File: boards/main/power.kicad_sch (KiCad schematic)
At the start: 19 parts, among them Q1 DMP2045U, U3 RT9080-33GJ5, U4 MCP73831T-2ACI_OT, U5 MAX17048G_T10

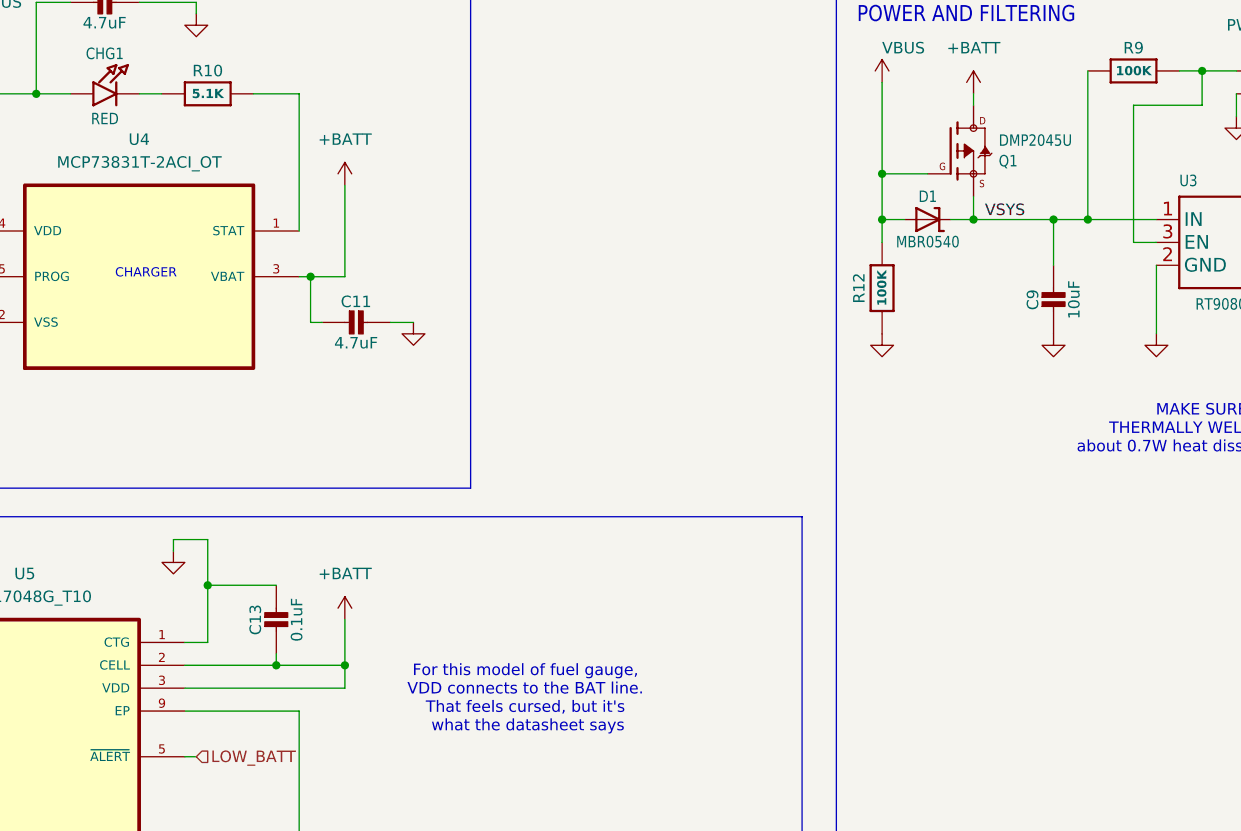
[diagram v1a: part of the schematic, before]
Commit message: Move the LED ring and haptic engine behind the charge controller, to prevent hot plug ringing from damaging things
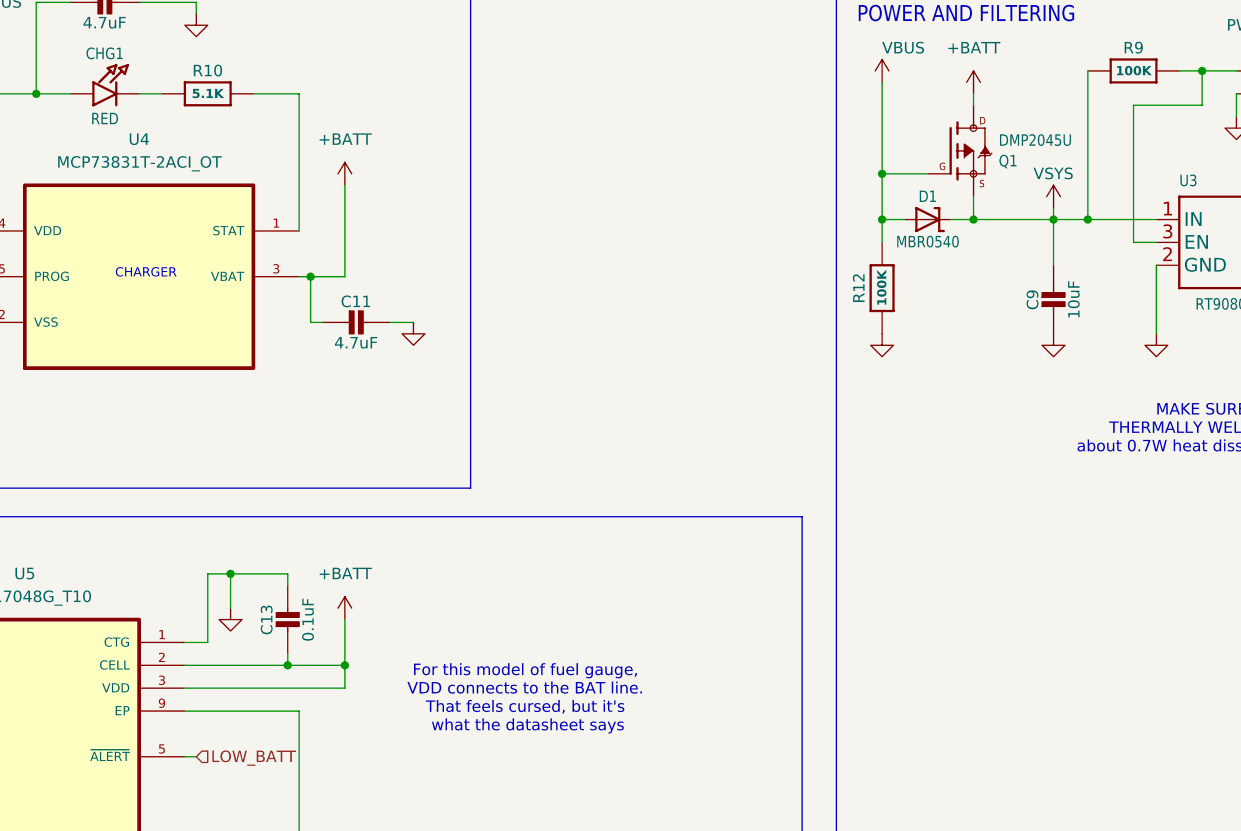
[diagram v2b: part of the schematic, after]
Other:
- moved on the sheet: C13
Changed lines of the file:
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@@
 	)
 	(junction
-		(at 78.74 96.52)
+		(at 93.98 105.41)
 		(diameter 0)
 		(color 0 0 0 0)
 	)
 	(junction
-		(at 93.98 105.41)
+		(at 153.67 55.88)
 		(diameter 0)
 		(color 0 0 0 0)
 	)
 	(junction
-		(at 153.67 55.88)
+		(at 87.63 105.41)
 		(diameter 0)
 		(color 0 0 0 0)
@@
 	)
 	(junction
-		(at 214.63 55.88)
+		(at 81.28 95.25)
 		(diameter 0)
 		(color 0 0 0 0)
 	)
 	(junction
-		(at 53.34 41.91)
+		(at 214.63 55.88)
 		(diameter 0)
 		(color 0 0 0 0)
 	)
 	(junction
-		(at 88.9 128.27)
+		(at 53.34 41.91)
 		(diameter 0)
 		(color 0 0 0 0)
 	)
 	(junction
-		(at 189.23 39.37)
+		(at 88.9 128.27)
 		(diameter 0)
 		(color 0 0 0 0)
 	)
 	(junction
-		(at 86.36 105.41)
+		(at 189.23 39.37)
 		(diameter 0)
 		(color 0 0 0 0)
@@
 	(wire
 		(pts
+			(xy 81.28 95.25) (xy 87.63 95.25)
+		)
+		(stroke
+			(width 0)
+			(type default)
+		)
+	)
+	(wire
+		(pts
 			(xy 93.98 107.95) (xy 93.98 105.41)
 		)
@@
 	(wire
 		(pts
-			(xy 78.74 96.52) (xy 78.74 102.87)
+			(xy 78.74 95.25) (xy 78.74 102.87)
+		)
+		(stroke
+			(width 0)
+			(type default)
+		)
+	)
+	(wire
+		(pts
+			(xy 87.63 95.25) (xy 87.63 96.52)
 		)
 		(stroke
@@
 	(wire
 		(pts
-			(xy 78.74 91.44) (xy 78.74 96.52)
-		)
-		(stroke
-			(width 0)
-			(type default)
-		)
-	)
-	(wire
-		(pts
 			(xy 49.53 62.23) (xy 53.34 62.23)
 		)
@@
 	(wire
 		(pts
-			(xy 78.74 96.52) (xy 86.36 96.52)
-		)
-		(stroke
-			(width 0)
-			(type default)
-		)
-	)
-	(wire
-		(pts
 			(xy 90.17 62.23) (xy 90.17 67.31)
 		)
@@
 	(wire
 		(pts
+			(xy 87.63 105.41) (xy 93.98 105.41)
+		)
+		(stroke
+			(width 0)
+			(type default)
+		)
+	)
+	(wire
+		(pts
 			(xy 214.63 68.58) (xy 214.63 71.12)
 		)
@@
 	(wire
 		(pts
-			(xy 76.2 105.41) (xy 86.36 105.41)
+			(xy 76.2 105.41) (xy 87.63 105.41)
 		)
 		(stroke
@@
 	(wire
 		(pts
-			(xy 74.93 91.44) (xy 78.74 91.44)
+			(xy 78.74 95.25) (xy 81.28 95.25)
 		)
 		(stroke
@@
 	(wire
 		(pts
+			(xy 172.72 54.61) (xy 172.72 55.88)
+		)
+		(stroke
+			(width 0)
+			(type default)
+		)
+	)
+	(wire
+		(pts
 			(xy 59.69 41.91) (xy 53.34 41.91)
 		)
@@
 	(wire
 		(pts
-			(xy 74.93 91.44) (xy 74.93 92.71)
+			(xy 81.28 95.25) (xy 81.28 99.06)
 		)
 		(stroke
@@
 	(wire
 		(pts
-			(xy 86.36 105.41) (xy 93.98 105.41)
-		)
-		(stroke
-			(width 0)
-			(type default)
-		)
-	)
-	(wire
-		(pts
 			(xy 181.61 43.18) (xy 181.61 58.42)
 		)
@@
 	(wire
 		(pts
-			(xy 86.36 104.14) (xy 86.36 105.41)
+			(xy 87.63 104.14) (xy 87.63 105.41)
 		)
 		(stroke
@@
 		)
 	)
-	(label "VSYS"
-		(at 165.1 55.88 0)
-		(effects
-			(font
-				(size 1.27 1.27)
-			)
-			(justify left bottom)
-		)
-	)
 	(hierarchical_label "SCL"
 		(shape input)
@@
 	(symbol
 		(lib_id "smart_compass_main:CAP_CERAMIC0603_NO")
-		(at 86.36 101.6 0)
+		(at 87.63 101.6 0)
 		(unit 1)
 		(body_style 1)
@@
 		(dnp no)
 		(property "Reference" "C13"
-			(at 84.07 100.35 90)
+			(at 85.34 100.35 90)
 			(show_name no)
 			(do_not_autoplace no)
@@
 		)
 		(property "Value" "0.1uF"
-			(at 88.66 100.35 90)
+			(at 89.93 100.35 90)
 			(show_name no)
 			(do_not_autoplace no)
@@
 		)
 		(property "Footprint" "Capacitor_SMD:C_0402_1005Metric"
-			(at 86.36 101.6 0)
+			(at 87.63 101.6 0)
 			(hide yes)
 			(show_name no)
@@
 		)
 		(property "Datasheet" "https://media.digikey.com/pdf/Data%20Sheets/Samsung%20PDFs/CL05B104KO5VPNC_Spec.pdf"
-			(at 86.36 101.6 0)
+			(at 87.63 101.6 0)
 			(hide yes)
 			(show_name no)
@@
 		)
 		(property "Description" ""
-			(at 86.36 101.6 0)
+			(at 87.63 101.6 0)
 			(hide yes)
 			(show_name no)
@@
 		)
 		(property "MPN" "CL05B104KO5VPNC"
-			(at 86.36 101.6 90)
+			(at 87.63 101.6 90)
 			(hide yes)
 			(show_name no)
@@
 		)
 		(property "PRICE" "0.02134"
-			(at 86.36 101.6 90)
+			(at 87.63 101.6 90)
 			(hide yes)
 			(show_name no)
@@
 		)
 		(property "MAXIMUM_PACKAGE_HIEGHT" ""
-			(at 86.36 101.6 90)
+			(at 87.63 101.6 90)
 			(hide yes)
 			(show_name no)
@@
 		)
 		(property "Manufacturer" "Samsung Electro-Mechanics"
-			(at 86.36 101.6 0)
+			(at 87.63 101.6 0)
 			(hide yes)
 			(show_name no)
@@
 		)
 		(property "DigiKey_PN" "1276-6844-1-ND"
-			(at 86.36 101.6 0)
+			(at 87.63 101.6 0)
 			(hide yes)
 			(show_name no)
@@
 		)
 		(property "Voltage" "16V"
-			(at 86.36 101.6 0)
+			(at 87.63 101.6 0)
 			(hide yes)
 			(show_name no)
@@
 		)
 		(property "Dielectric" "X7R"
-			(at 86.36 101.6 0)
+			(at 87.63 101.6 0)
 			(hide yes)
 			(show_name no)
@@
 		)
 		(property "DigiKey_Part_Number" ""
-			(at 86.36 101.6 90)
+			(at 87.63 101.6 90)
 			(hide yes)
 			(show_name no)
@@
 	(symbol
 		(lib_id "power:GND")
-		(at 74.93 92.71 0)
+		(at 81.28 99.06 0)
 		(unit 1)
 		(body_style 1)
@@
 		(fields_autoplaced yes)
 		(property "Reference" "#PWR038"
-			(at 74.93 99.06 0)
+			(at 81.28 105.41 0)
 			(hide yes)
 			(show_name no)
@@
 		)
 		(property "Value" "GND"
-			(at 74.93 97.79 0)
+			(at 81.28 104.14 0)
 			(hide yes)
 			(show_name no)
@@
 		)
 		(property "Footprint" ""
-			(at 74.93 92.71 0)
+			(at 81.28 99.06 0)
 			(hide yes)
 			(show_name no)
@@
 		)
 		(property "Datasheet" ""
-			(at 74.93 92.71 0)
+			(at 81.28 99.06 0)
 			(hide yes)
 			(show_name no)
@@
 		)
 		(property "Description" "Power symbol creates a global label with name \"GND\" , ground"
-			(at 74.93 92.71 0)
+			(at 81.28 99.06 0)
 			(hide yes)
 			(show_name no)
@@
 					(unit 1)
 				)
+			)
+		)
+	)
+	(symbol
+		(lib_id "power:+BATT")
+		(at 172.72 54.61 0)
+		(unit 1)
+		(body_style 1)
+		(exclude_from_sim no)
+		(in_bom yes)
+		(on_board yes)
+		(in_pos_files yes)
+		(dnp no)
+		(property "Reference" "#PWR079"
+			(at 172.72 58.42 0)
+			(hide yes)
+			(show_name no)
+			(do_not_autoplace no)
+			(effects
+				(font
+					(size 1.27 1.27)
+				)
+			)
+		)
+		(property "Value" "VSYS"
+			(at 172.72 50.8 0)
+			(show_name no)
+			(do_not_autoplace no)
+			(effects
+				(font
+					(size 1.27 1.27)
+				)
+			)
+		)
+		(property "Footprint" ""
+			(at 172.72 54.61 0)
+			(hide yes)
+			(show_name no)
+			(do_not_autoplace no)
+			(effects
+				(font
+					(size 1.27 1.27)
+				)
+			)
+		)
+		(property "Datasheet" ""
+			(at 172.72 54.61 0)
+			(hide yes)
+			(show_name no)
+			(do_not_autoplace no)
+			(effects
+				(font
+					(size 1.27 1.27)
+				)
+			)
+		)
+		(property "Description" "Power symbol creates a global label with name \"+BATT\""
+			(at 172.72 54.61 0)
+			(hide yes)
+			(show_name no)
+			(do_not_autoplace no)
+			(effects
+				(font
+					(size 1.27 1.27)
+				)
+			)
+		)
+		(pin "1"
+		)
+		(instances
+			(project "SmartCompass"
+				(path "/0c161f28-8075-4403-a867-35208f463636/44fc6246-5945-463a-870f-e1f278c176e3"
+					(reference "#PWR079")
+					(unit 1)
+				)

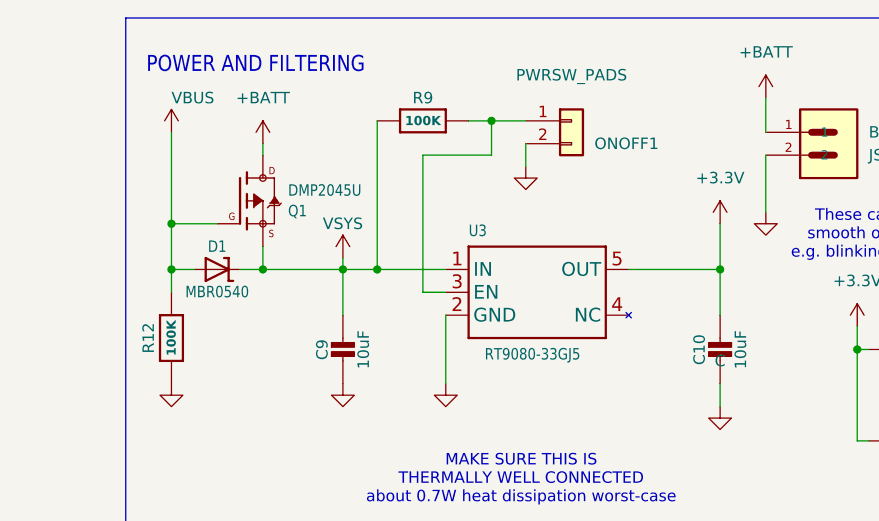
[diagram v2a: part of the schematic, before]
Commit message: Update components based on spice sim. Added another load-sharing schottky diode
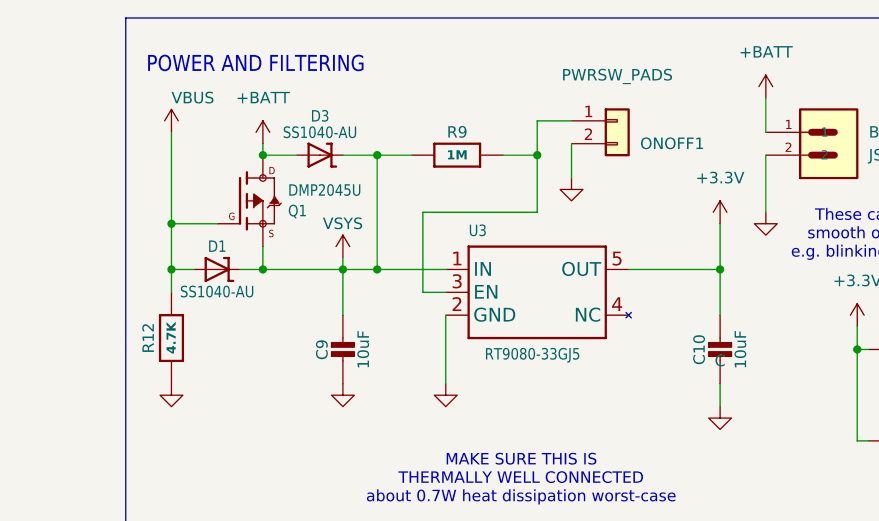
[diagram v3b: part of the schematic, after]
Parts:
- added D3: SS1040-AU, Diode_SMD:D_SOD-123, symbol smart_compass_main:DIODE-SCHOTTKYSOD-123
- D1: value MBR0540 -> SS1040-AU; DigiKey_PN MBR0540TPMSCT-ND -> 3757-SS1040-AU_R1_000A1CT-ND; MPN MBR0540-TP -> SS1040-AU_R1_000A1; Manufacturer MCC (Micro Commercial Components) -> Panjit International Inc.; PRICE 0.23 -> 0.18
- Q1: Sourcing_Note P-channel power mux between the battery and the LDO input: drain on +BATT, source on the LDO rail, gate on VBUS with a 100k pulldown, paired with the MBR0540 Schottky that feeds the rail from USB. Replaces the DMG3415U-7, which the manufacturer marks NOT RECOMMENDED FOR NEW DESIGN and names this part as its successor. Same SOT-23 package and same G/S/D pinout, so the swap needs no layout change. Package is JEDEC TO-236AB: 2.90 x 1.30mm body, 2.40mm lead span, 0.95mm pitch, which is what Package_TO_SOT_SMD:SOT-23 is drawn for. The earlier footprint, SOT95P240X105-3N, had the same outline but lived in a per-part library that is no longer present, which is why this field had gone empty. Rds(on) is slightly higher than the old part (45mOhm vs 39mOhm at 4.5V drive, 90mOhm vs 71mOhm at 1.8V) and Ciss roughly doubles to 634pF, but neither matters here: the FET carries only the 3.3V LDO input current, a few hundred mA at most, since the LED ring's boost taps +BATT upstream through FB1. Conduc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 -> P-channel power mux between the battery and the LDO input: drain on +BATT, source on VSYS, gate on VBUS with a 4.7k pulldown, paired with the SS1040-AU Schottky that feeds VSYS from USB. A second SS1040-AU sits across drain and source so the cell feeds VSYS through a Schottky rather than the body diode while the gate waits for VBUS to drain after unplugging; without it the 3.3V rail can dip below 2.7V for about 10ms with a low cell and a bright LED ring (see boards/main/sim/RESULTS.md). Replaces the DMG3415U-7, which the manufacturer marks NOT RECOMMENDED FOR NEW DESIGN and names this part as its successor. Same SOT-23 package and same G/S/D pinout. Package is JEDEC TO-236AB: 2.90 x 1.30mm body, 2.40mm lead span, 0.95mm pitch, which is what Package_TO_SOT_SMD:SOT-23 is drawn for. Carries the whole VSYS load on battery, the LDO and the LED ring's boost, up to about 0.6A; at 45mOhm that is under 20mW against an 800mW rating.
- R12: value 100K -> 4.7K; DigiKey_PN 311-100KHRCT-ND -> 311-4.70KHRCT-ND; MPN RC0603FR-07100KL -> RC0603FR-074K7L
- R9: value 100K -> 1M; DigiKey_PN 311-100KHRCT-ND -> 311-1.00MHRCT-ND; MPN RC0603FR-07100KL -> RC0603FR-071ML
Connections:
- net +BATT: now also D3.2 (A)
- net GND: now also R12.2; no longer R12.1
- net VBUS: now also R12.1; no longer R12.2
- net VSYS: now also D3.1 (K)
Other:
- moved on the sheet: ONOFF1, R9
